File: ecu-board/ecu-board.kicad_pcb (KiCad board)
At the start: 2 copper layers, 150 x 100 mm, 44 parts, among them J1 MicroSquirt_connector, J10 Injector connector, J11 Cockpit connector, J12 EGO connector, J13 Chrankshaft Hall connector, J14 Camshaft Hall connector, J15 Ignition 1 connector, J16 Ignition 2 connector, J17 Camera connector, J18 Wheel Hall connector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

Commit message: Ignore lib cache files.
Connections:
- K1 pad 30: (no net) -> +BATT
- K1 pad 85: (no net) -> GNDS
- K1 pad 86: (no net) -> /button_to_main_relay
- K1 pad 87: (no net) -> +12V
- K1 pad 87a: (no net) -> Net-(K1-Pad87a)
- K2 pad 30: (no net) -> +12V
- K2 pad 85: (no net) -> /button_to_start_motor_relay
- K2 pad 86: (no net) -> +12V
- K2 pad 87: (no net) -> /relay_to_start_motor
- K2 pad 87a: (no net) -> Net-(K2-Pad87a)
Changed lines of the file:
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@@
     (zones 0)
     (modules 44)
-    (nets 62)
+    (nets 64)
   )
   (page A4)
@@
   (net 60 "Net-(U1-Pad5)")
   (net 61 "Net-(U1-Pad4)")
+  (net 62 "Net-(K1-Pad87a)")
+  (net 63 "Net-(K2-Pad87a)")
   (net_class Default "This is the default net class."
     (clearance 0.2)
@@
     (add_net "Net-(J5-Pad8)")
     (add_net "Net-(J5-Pad9)")
+    (add_net "Net-(K1-Pad87a)")
+    (add_net "Net-(K2-Pad87a)")
     (add_net "Net-(U1-Pad4)")
     (add_net "Net-(U1-Pad5)")
@@
     (fp_line (start 13 17) (end 13 -12) (layer F.CrtYd) (width 0.12))
     (fp_line (start 13 -12) (end -13 -12) (layer F.CrtYd) (width 0.12))
-    (pad 87a thru_hole circle (at 0 0) (size 4 4) (drill 2.5) (layers *.Cu *.Mask))
-    (pad 87 thru_hole circle (at 0 -8) (size 4 4) (drill 2.5) (layers *.Cu *.Mask))
-    (pad 30 thru_hole circle (at 0 10.2) (size 4 4) (drill 2.5) (layers *.Cu *.Mask))
-    (pad 85 thru_hole circle (at -8.7 0.7) (size 4 4) (drill 2.5) (layers *.Cu *.Mask))
-    (pad 86 thru_hole circle (at 8.7 0.7) (size 4 4) (drill 2.5) (layers *.Cu *.Mask))
+    (pad 87a thru_hole circle (at 0 0) (size 4 4) (drill 2.5) (layers *.Cu *.Mask)
+      (net 62 "Net-(K1-Pad87a)"))
+    (pad 87 thru_hole circle (at 0 -8) (size 4 4) (drill 2.5) (layers *.Cu *.Mask)
+      (net 6 +12V))
+    (pad 30 thru_hole circle (at 0 10.2) (size 4 4) (drill 2.5) (layers *.Cu *.Mask)
+      (net 30 +BATT))
+    (pad 85 thru_hole circle (at -8.7 0.7) (size 4 4) (drill 2.5) (layers *.Cu *.Mask)
+      (net 4 GNDS))
+    (pad 86 thru_hole circle (at 8.7 0.7) (size 4 4) (drill 2.5) (layers *.Cu *.Mask)
+      (net 3 /button_to_main_relay))
     (pad "" np_thru_hole circle (at -6.5 8.2) (size 2 2) (drill 2) (layers *.Cu *.Mask))
     (pad "" np_thru_hole circle (at 6.5 -5.8) (size 2 2) (drill 2) (layers *.Cu *.Mask))
@@
     (pad "" np_thru_hole circle (at 6.5 -5.8) (size 2 2) (drill 2) (layers *.Cu *.Mask))
     (pad "" np_thru_hole circle (at -6.5 8.2) (size 2 2) (drill 2) (layers *.Cu *.Mask))
-    (pad 86 thru_hole circle (at 8.7 0.7) (size 4 4) (drill 2.5) (layers *.Cu *.Mask))
-    (pad 85 thru_hole circle (at -8.7 0.7) (size 4 4) (drill 2.5) (layers *.Cu *.Mask))
-    (pad 30 thru_hole circle (at 0 10.2) (size 4 4) (drill 2.5) (layers *.Cu *.Mask))
-    (pad 87 thru_hole circle (at 0 -8) (size 4 4) (drill 2.5) (layers *.Cu *.Mask))
-    (pad 87a thru_hole circle (at 0 0) (size 4 4) (drill 2.5) (layers *.Cu *.Mask))
+    (pad 86 thru_hole circle (at 8.7 0.7) (size 4 4) (drill 2.5) (layers *.Cu *.Mask)
+      (net 6 +12V))
+    (pad 85 thru_hole circle (at -8.7 0.7) (size 4 4) (drill 2.5) (layers *.Cu *.Mask)
+      (net 5 /button_to_start_motor_relay))
+    (pad 30 thru_hole circle (at 0 10.2) (size 4 4) (drill 2.5) (layers *.Cu *.Mask)
+      (net 6 +12V))
+    (pad 87 thru_hole circle (at 0 -8) (size 4 4) (drill 2.5) (layers *.Cu *.Mask)
+      (net 2 /relay_to_start_motor))
+    (pad 87a thru_hole circle (at 0 0) (size 4 4) (drill 2.5) (layers *.Cu *.Mask)
+      (net 63 "Net-(K2-Pad87a)"))
   )
   (module ecu-board-footprints:SOT1852-1 (layer F.Cu)

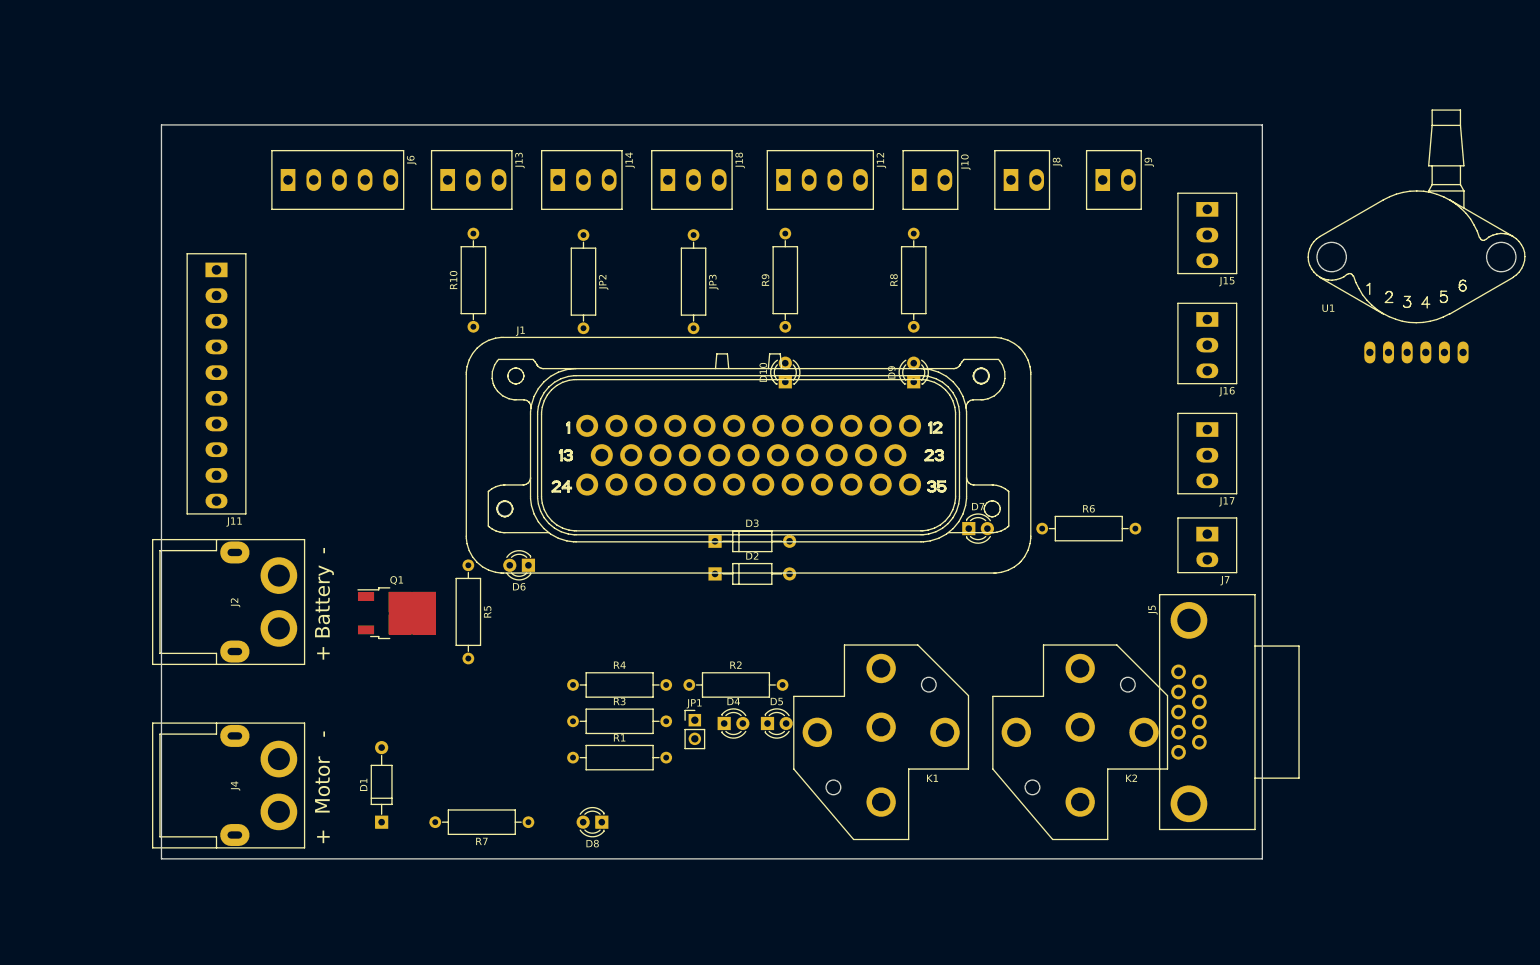
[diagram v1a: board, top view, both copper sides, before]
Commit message: Change from 3.50mm to 5.00mm terminal blocks.
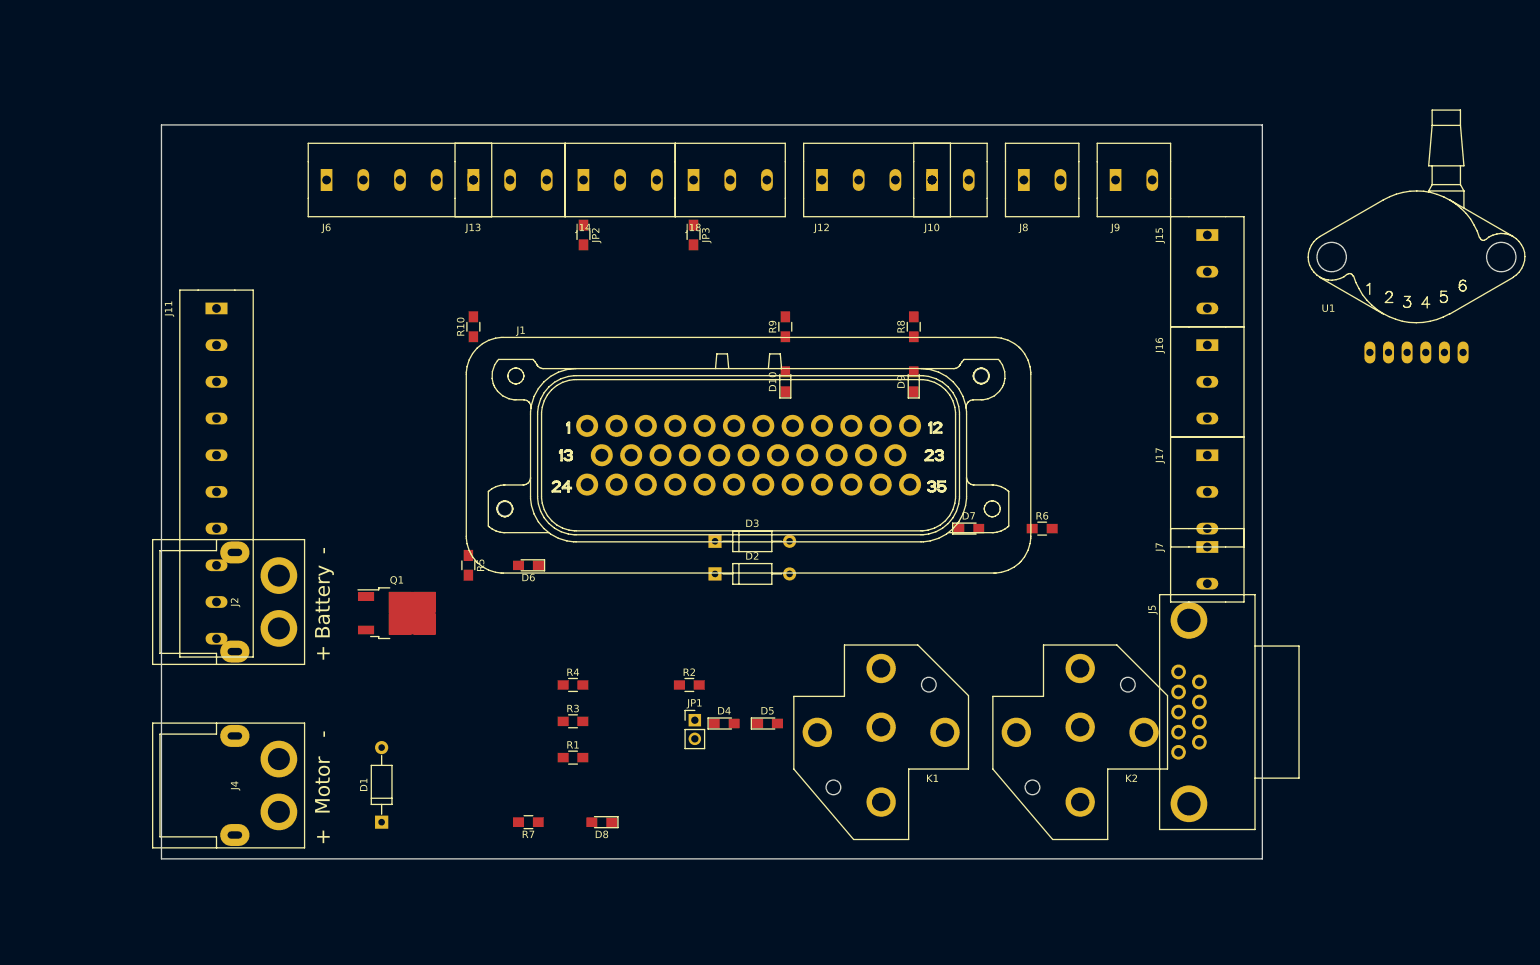
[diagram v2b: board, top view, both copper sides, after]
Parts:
- D10, D4, D5, D6, D7, D8, D9: footprint LEDs:LED_D3.0mm -> LEDs:LED_0805_HandSoldering
- J10, J7, J8, J9: footprint ecu-board-footprints:Wurth_2141_02x3.5mm -> ecu-board-footprints:Terminal_Block_2x5.00mm
- J11: footprint ecu-board-footprints:Wurth_2141_10x3.5mm -> ecu-board-footprints:Terminal_Block_10x5.00mm
- J12: footprint ecu-board-footprints:Wurth_2141_04x3.5mm -> ecu-board-footprints:Terminal_Block_4x5.00mm
- J13, J14, J15, J16, J17, J18: footprint ecu-board-footprints:Wurth_2141_03x3.5mm -> ecu-board-footprints:Terminal_Block_3x5.00mm
- J6: footprint ecu-board-footprints:Wurth_2141_05x3.5mm -> ecu-board-footprints:Terminal_Block_5x5.00mm
- JP2, JP3, R1, R10, R2, R3, R4, R5, R6, R7, R8, R9: footprint Resistors_THT:R_Axial_DIN0309_L9.0mm_D3.2mm_P12.70mm_Horizontal -> Resistors_SMD:R_0805_HandSoldering

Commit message: Import fuse holders to pcb.
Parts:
- added F1: 3A Fuse, ecu-board-footprints:Fuseholder_ATO_Blade_Littelfuse_Pudenz_4_Pin, F.Cu at (40.1, 90.5)
- added F2: 5A Fuse, ecu-board-footprints:Fuseholder_ATO_Blade_Littelfuse_Pudenz_4_Pin, F.Cu at (40.1, 97.6)
- added F4: 5A Fuse, ecu-board-footprints:Fuseholder_ATO_Blade_Littelfuse_Pudenz_4_Pin, F.Cu at (40.1, 64.1)
- added F5: 5A Fuse, ecu-board-footprints:Fuseholder_ATO_Blade_Littelfuse_Pudenz_4_Pin, F.Cu at (40.1, 71.2)
- added F6: 3A Fuse, ecu-board-footprints:Fuseholder_ATO_Blade_Littelfuse_Pudenz_4_Pin, F.Cu at (40.1, 78.4)

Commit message: Layout fuses.
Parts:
- moved F6 157.6 mm to (195.0, 107.5)
- moved F4 136.2 mm to (176.2, 61.4), turned to 90 degrees
- moved F5 115.3 mm to (155.0, 62.5), turned to 90 degrees
- moved F2 80.7 mm to (115.0, 127.5), turned to 90 degrees
- moved F1 45.0 mm to (85.0, 87.5), turned to 90 degrees
- moved U1 38.8 mm to (187.5, 87.5)
- moved J15 24.6 mm to (215.0, 55.0)
- moved J16 23.7 mm to (215.0, 72.5)
- moved J5 23.6 mm to (213.5, 132.5)
- moved J17 23.0 mm to (215.0, 90.0)
- moved J7 22.5 mm to (215.0, 107.5)
- moved J10 21.5 mm to (172.5, 45.0)
- moved J8 21.5 mm to (185.0, 45.0)
- moved J9 21.5 mm to (197.5, 45.0)
- moved J11 20.0 mm to (57.5, 55.0)
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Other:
- board size 150 x 100 mm -> 175 x 115 mm

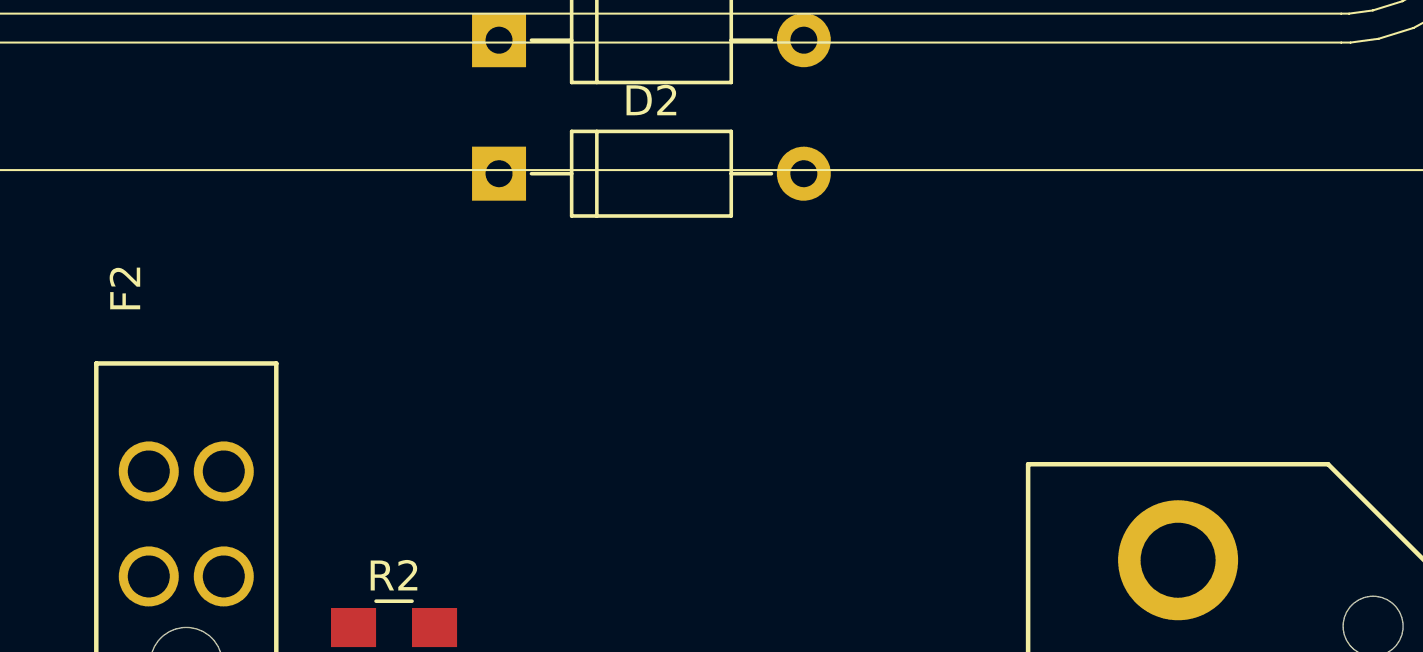
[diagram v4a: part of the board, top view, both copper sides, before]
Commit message: Add breakout connector.
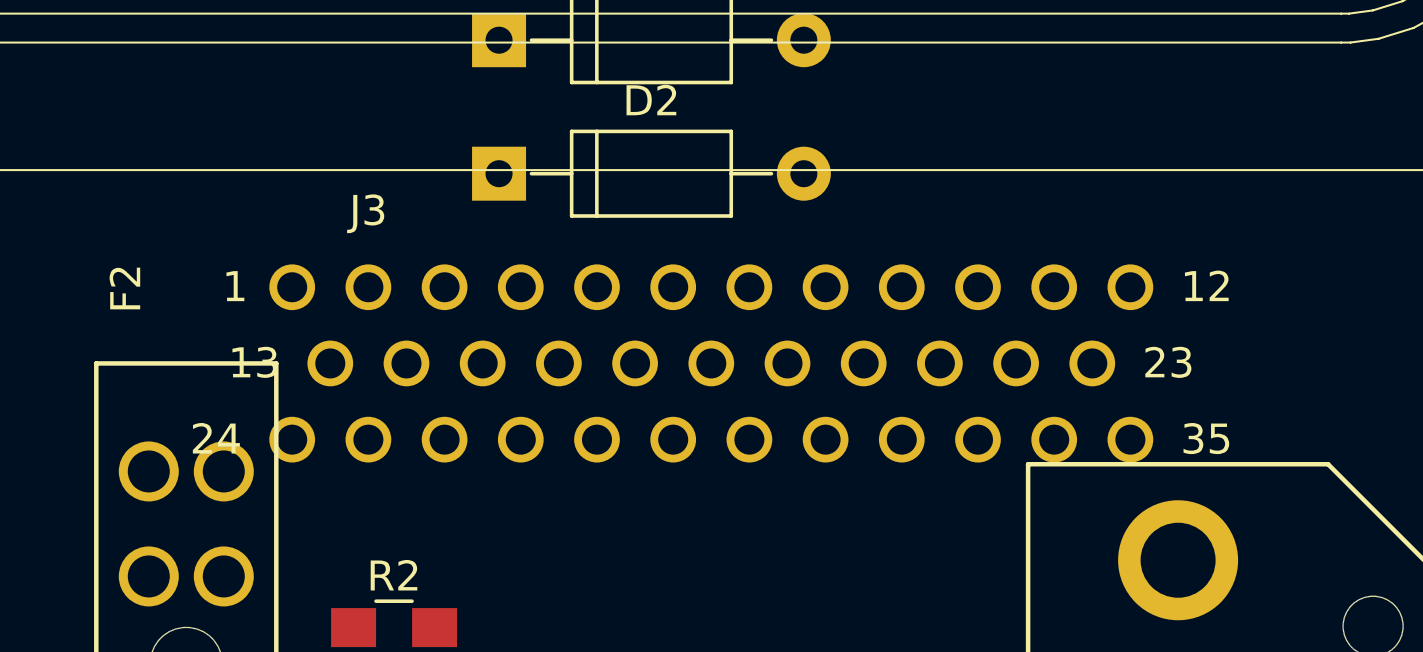
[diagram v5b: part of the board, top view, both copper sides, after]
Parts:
- added J3: MS_breakout_conn, ecu-board-footprints:MicroSquirt_35Pin, F.Cu at (132.5, 117.5)
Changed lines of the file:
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@@
     (tracks 0)
     (zones 0)
-    (modules 49)
+    (modules 50)
     (nets 64)
   )
@@
     (pad "" np_thru_hole circle (at 0 0) (size 2.4 2.4) (drill 2.4) (layers *.Cu *.Mask))
   )
+  (module ecu-board-footprints:MicroSquirt_35Pin (layer F.Cu)
+    (at 132.5 117.5)
+    (fp_text reference J3 (at -11.43 -5.08) (layer F.SilkS)
+      (effects (font (size 1 1) (thickness 0.15)))
+    )
+    (fp_text value MS_breakout_conn (at 0 5.08) (layer F.Fab)
+      (effects (font (size 1 1) (thickness 0.15)))
+    )
+    (fp_text user 1 (at -15.875 -2.54) (layer F.SilkS)
+      (effects (font (size 1 1) (thickness 0.15)))
+    )
+    (fp_text user 12 (at 16.51 -2.54) (layer F.SilkS)
+      (effects (font (size 1 1) (thickness 0.15)))
+    )
+    (fp_text user 13 (at -15.24 0) (layer F.SilkS)
+      (effects (font (size 1 1) (thickness 0.15)))
+    )
+    (fp_text user 23 (at 15.24 0) (layer F.SilkS)
+      (effects (font (size 1 1) (thickness 0.15)))
+    )
+    (fp_text user 35 (at 16.51 2.54) (layer F.SilkS)
+      (effects (font (size 1 1) (thickness 0.15)))
+    )
+    (fp_text user 24 (at -16.51 2.54) (layer F.SilkS)
+      (effects (font (size 1 1) (thickness 0.15)))
+    )
+    (pad 1 thru_hole circle (at -13.97 -2.54) (size 1.524 1.524) (drill 1) (layers *.Cu *.Mask)
+      (net 41 "Net-(F2-Pad1)"))
+    (pad 2 thru_hole circle (at -11.43 -2.54) (size 1.524 1.524) (drill 1) (layers *.Cu *.Mask)
+      (net 44 /CANH))
+    (pad 3 thru_hole circle (at -8.89 -2.54) (size 1.524 1.524) (drill 1) (layers *.Cu *.Mask)
+      (net 45 /CANL))
+    (pad 4 thru_hole circle (at -6.35 -2.54) (size 1.524 1.524) (drill 1) (layers *.Cu *.Mask)
+      (net 46 /VRIN2+))
+    (pad 5 thru_hole circle (at -3.81 -2.54) (size 1.524 1.524) (drill 1) (layers *.Cu *.Mask)
+      (net 47 /spare_in2))
+    (pad 6 thru_hole circle (at -1.27 -2.54) (size 1.524 1.524) (drill 1) (layers *.Cu *.Mask)
+      (net 48 /flex_fuel))
+    (pad 7 thru_hole circle (at 1.27 -2.54) (size 1.524 1.524) (drill 1) (layers *.Cu *.Mask)
+      (net 49 /fidle))
+    (pad 8 thru_hole circle (at 3.81 -2.54) (size 1.524 1.524) (drill 1) (layers *.Cu *.Mask)
+      (net 50 /fuel_pump))
+    (pad 9 thru_hole circle (at 6.35 -2.54) (size 1.524 1.524) (drill 1) (layers *.Cu *.Mask)
+      (net 28 /injector_1))
+    (pad 10 thru_hole circle (at 8.89 -2.54) (size 1.524 1.524) (drill 1) (layers *.Cu *.Mask)
+      (net 51 /injector_2))
+    (pad 11 thru_hole circle (at 11.43 -2.54) (size 1.524 1.524) (drill 1) (layers *.Cu *.Mask)
+      (net 38 /ignition_2))
+    (pad 12 thru_hole circle (at 13.97 -2.54) (size 1.524 1.524) (drill 1) (layers *.Cu *.Mask)
+      (net 37 /ignition_1))
+    (pad 12 thru_hole circle (at 13.97 -2.54) (size 1.524 1.524) (drill 1) (layers *.Cu *.Mask)
+      (net 37 /ignition_1))
+    (pad 13 thru_hole circle (at -12.7 0) (size 1.524 1.524) (drill 1) (layers *.Cu *.Mask)
+      (net 16 /serial_RX))
+    (pad 14 thru_hole circle (at -10.16 0) (size 1.524 1.524) (drill 1) (layers *.Cu *.Mask)
+      (net 17 /serial_TX))
+    (pad 15 thru_hole circle (at -7.62 0) (size 1.524 1.524) (drill 1) (layers *.Cu *.Mask)
+      (net 39 /bootload))
+    (pad 16 thru_hole circle (at -5.08 0) (size 1.524 1.524) (drill 1) (layers *.Cu *.Mask)
+      (net 52 /accel_led))
+    (pad 17 thru_hole circle (at -2.54 0) (size 1.524 1.524) (drill 1) (layers *.Cu *.Mask)
+      (net 53 /warm-up))
+    (pad 18 thru_hole circle (at 0 0) (size 1.524 1.524) (drill 1) (layers *.Cu *.Mask)
+      (net 4 GNDS))
+    (pad 19 thru_hole circle (at 2.54 0) (size 1.524 1.524) (drill 1) (layers *.Cu *.Mask)
+      (net 4 GNDS))
+    (pad 20 thru_hole circle (at 5.08 0) (size 1.524 1.524) (drill 1) (layers *.Cu *.Mask)
+      (net 4 GNDS))
+    (pad 21 thru_hole circle (at 7.62 0) (size 1.524 1.524) (drill 1) (layers *.Cu *.Mask)
+      (net 36 /cam_hall_signal))
+    (pad 22 thru_hole circle (at 10.16 0) (size 1.524 1.524) (drill 1) (layers *.Cu *.Mask)
+      (net 1 GNDPWR))
+    (pad 23 thru_hole circle (at 12.7 0) (size 1.524 1.524) (drill 1) (layers *.Cu *.Mask)
+      (net 1 GNDPWR))
+    (pad 24 thru_hole circle (at -13.97 2.54) (size 1.524 1.524) (drill 1) (layers *.Cu *.Mask)
+      (net 54 /map_signal))
+    (pad 25 thru_hole circle (at -11.43 2.54) (size 1.524 1.524) (drill 1) (layers *.Cu *.Mask)
+      (net 27 /clt_signal))
+    (pad 26 thru_hole circle (at -8.89 2.54) (size 1.524 1.524) (drill 1) (layers *.Cu *.Mask)
+      (net 26 /iat_signal))
+    (pad 27 thru_hole circle (at -6.35 2.54) (size 1.524 1.524) (drill 1) (layers *.Cu *.Mask)
+      (net 43 /TPS_input))
+    (pad 28 thru_hole circle (at -3.81 2.54) (size 1.524 1.524) (drill 1) (layers *.Cu *.Mask)
+      (net 42 +5V))
+    (pad 29 thru_hole circle (at -1.27 2.54) (size 1.524 1.524) (drill 1) (layers *.Cu *.Mask)
+      (net 55 /spare_in1))
+    (pad 30 thru_hole circle (at 1.27 2.54) (size 1.524 1.524) (drill 1) (layers *.Cu *.Mask)
+      (net 56 /opto_in+))
+    (pad 31 thru_hole circle (at 3.81 2.54) (size 1.524 1.524) (drill 1) (layers *.Cu *.Mask)
+      (net 57 /opto_in-))
+    (pad 32 thru_hole circle (at 6.35 2.54) (size 1.524 1.524) (drill 1) (layers *.Cu *.Mask)
+      (net 58 /VRIN1+))
+    (pad 33 thru_hole circle (at 8.89 2.54) (size 1.524 1.524) (drill 1) (layers *.Cu *.Mask)
+      (net 35 /crank_hall_signal))
+    (pad 34 thru_hole circle (at 11.43 2.54) (size 1.524 1.524) (drill 1) (layers *.Cu *.Mask)
+      (net 34 /ego_signal))
+    (pad 35 thru_hole circle (at 13.97 2.54) (size 1.524 1.524) (drill 1) (layers *.Cu *.Mask)
+      (net 23 /tachometer))
+  )
   (gr_line (start 225 35) (end 50 35) (layer Edge.Cuts) (width 0.05))
